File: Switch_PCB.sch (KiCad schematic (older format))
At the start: 53 parts, among them J1 Black, J10 Black, J11 Red, J12-1 Jack 2.1mm, J12-2 Jack 2.1mm, J13 Black, J14 Red, J15 Black, J16 Red, J17 Black, J18 Red, J19 Black, J2 Red, J20 Red, J21 Black, J22 Red, J23 Black, J24 Red, J25 Black, J26 Red, J27 Black, J28 Red, J3 Black, J4 Red, J5 Black, J6 Red, J7 Black, J8 Red, J9 Red, SW1 Switch On-Off-On, SW2 Switch On-Off-On, SW3 Switch On-Off-On, SW4 Switch On-Off-On

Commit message: - validation schématique - validation du contour du PCB - validation du placement des composants, verrouillage des empreintes correctement positionnées
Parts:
- added J12-0: Conn_01x02, Connector_PinHeader_2.54mm:PinHeader_1x02_P2.54mm_Horizontal, symbol Connector_Generic:Conn_01x02
- J1, J3, J5, J7: Description GND -> Alim 1 -
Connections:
- net labels added: +5VD, +VDC, GNDD, GNDPWR
- net labels removed: +5V, GND1, GND2
- wire segments 125 -> 128
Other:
- note added: "KiCad Power Flag for DRC"
- note added: "LED\nON"
- note added: "Mounting Holes"
- note added: "OSHW"
- note added: "Open Source Hardware"
- note removed: "KiCad Power DRC"
- moved on the sheet: H1, H2, H3, H4, J12-1, J12-2

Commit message: Update color for each Banana connector to the pcb component placement 3d rendered.
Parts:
- J1, J10, J21, J23, J25, J27, J3, J5, J7: footprint ArnauldDev_Connector_Banana:SCHUTZINGER_SWEB8094AU-SW_4mm_Horizontal -> ArnauldDev_Connector_Banana:SCHUTZINGER_SWEB8094AU-SW_4mm_Horizontal_Black
- J11, J2, J22, J24, J26, J28, J4, J6, J8, J9: footprint ArnauldDev_Connector_Banana:SCHUTZINGER_SWEB8094AU-SW_4mm_Horizontal -> ArnauldDev_Connector_Banana:SCHUTZINGER_SWEB8094AU-SW_4mm_Horizontal_Red
- J13, J15, J17, J19: footprint ArnauldDev_Connector_Banana:STAUBLI_66.9032-21_XELA-4_4mm_Vertical -> ArnauldDev_Connector_Banana:STAUBLI_66.9032-21_XELA-4_4mm_Vertical_Black
- J14, J16, J18, J20: footprint ArnauldDev_Connector_Banana:STAUBLI_66.9032-21_XELA-4_4mm_Vertical -> ArnauldDev_Connector_Banana:STAUBLI_66.9032-21_XELA-4_4mm_Vertical_Red

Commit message: - Add 3 pin conn for LED states - Start of the routing of the tracks of the electronic card
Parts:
- added J13, J14, J15, J16: Conn_01x03, Connector_PinHeader_2.54mm:PinHeader_1x03_P2.54mm_Vertical, symbol Connector_Generic:Conn_01x03
- J1, J10, J3, J5, J7: symbol Connector_Generic:Conn_01x01 -> Connector:Conn_Coaxial
- J11, J2, J4, J6, J8, J9: footprint ArnauldDev_Connector_Banana:SCHUTZINGER_SWEB8094AU-SW_4mm_Horizontal_Red -> ArnauldDev_Connector_Banana:SCHUTZINGER_SWEB8094AU-RT_4mm_Horizontal_Red; symbol Connector_Generic:Conn_01x01 -> Connector:Conn_Coaxial
- J19: renamed from J13; symbol Connector_Generic:Conn_01x01 -> Connector:Conn_Coaxial
- J20: renamed from J14; footprint ArnauldDev_Connector_Banana:STAUBLI_66.9032-21_XELA-4_4mm_Vertical_Red -> ArnauldDev_Connector_Banana:STAUBLI_66.9032-22_XELA-4_4mm_Vertical_Red; symbol Connector_Generic:Conn_01x01 -> Connector:Conn_Coaxial
- J21: renamed from J15; symbol Connector_Generic:Conn_01x01 -> Connector:Conn_Coaxial
- J22: renamed from J16; footprint ArnauldDev_Connector_Banana:STAUBLI_66.9032-21_XELA-4_4mm_Vertical_Red -> ArnauldDev_Connector_Banana:STAUBLI_66.9032-22_XELA-4_4mm_Vertical_Red; symbol Connector_Generic:Conn_01x01 -> Connector:Conn_Coaxial
- J23: renamed from J17; symbol Connector_Generic:Conn_01x01 -> Connector:Conn_Coaxial
- J24: renamed from J18; footprint ArnauldDev_Connector_Banana:STAUBLI_66.9032-21_XELA-4_4mm_Vertical_Red -> ArnauldDev_Connector_Banana:STAUBLI_66.9032-22_XELA-4_4mm_Vertical_Red; symbol Connector_Generic:Conn_01x01 -> Connector:Conn_Coaxial
- J25: renamed from J19; symbol Connector_Generic:Conn_01x01 -> Connector:Conn_Coaxial
- J26: renamed from J20; footprint ArnauldDev_Connector_Banana:STAUBLI_66.9032-21_XELA-4_4mm_Vertical_Red -> ArnauldDev_Connector_Banana:STAUBLI_66.9032-22_XELA-4_4mm_Vertical_Red; symbol Connector_Generic:Conn_01x01 -> Connector:Conn_Coaxial
- J27: renamed from J21; symbol Connector_Generic:Conn_01x01 -> Connector:Conn_Coaxial
- J28: renamed from J22; footprint ArnauldDev_Connector_Banana:SCHUTZINGER_SWEB8094AU-SW_4mm_Horizontal_Red -> ArnauldDev_Connector_Banana:SCHUTZINGER_SWEB8094AU-RT_4mm_Horizontal_Red; symbol Connector_Generic:Conn_01x01 -> Connector:Conn_Coaxial
- J29: renamed from J23; symbol Connector_Generic:Conn_01x01 -> Connector:Conn_Coaxial
- J30: renamed from J24; footprint ArnauldDev_Connector_Banana:SCHUTZINGER_SWEB8094AU-SW_4mm_Horizontal_Red -> ArnauldDev_Connector_Banana:SCHUTZINGER_SWEB8094AU-RT_4mm_Horizontal_Red; symbol Connector_Generic:Conn_01x01 -> Connector:Conn_Coaxial
- J31: renamed from J25; symbol Connector_Generic:Conn_01x01 -> Connector:Conn_Coaxial
- J32: renamed from J26; footprint ArnauldDev_Connector_Banana:SCHUTZINGER_SWEB8094AU-SW_4mm_Horizontal_Red -> ArnauldDev_Connector_Banana:SCHUTZINGER_SWEB8094AU-RT_4mm_Horizontal_Red; symbol Connector_Generic:Conn_01x01 -> Connector:Conn_Coaxial
- J33: renamed from J27; symbol Connector_Generic:Conn_01x01 -> Connector:Conn_Coaxial
- J34: renamed from J28; footprint ArnauldDev_Connector_Banana:SCHUTZINGER_SWEB8094AU-SW_4mm_Horizontal_Red -> ArnauldDev_Connector_Banana:SCHUTZINGER_SWEB8094AU-RT_4mm_Horizontal_Red; symbol Connector_Generic:Conn_01x01 -> Connector:Conn_Coaxial
- renumbered J12-0 to J12, J12-1 to J17, J12-2 to J18
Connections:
- net GNDD: now also J13.1 (Pin_1), J14.1 (Pin_1), J15.1 (Pin_1), J16.1 (Pin_1)
- net GNDPWR: now also J1.2 (Ext), J10.2 (Ext), J11.2 (Ext), J19.2 (Ext), J2.2 (Ext), J20.2 (Ext), J21.2 (Ext), J22.2 (Ext), J23.2 (Ext), J24.2 (Ext), J25.2 (Ext), J26.2 (Ext), J27.2 (Ext), J28.2 (Ext), J29.2 (Ext), J3.2 (Ext), J30.2 (Ext), J31.2 (Ext), J32.2 (Ext), J33.2 (Ext), J34.2 (Ext), J4.2 (Ext), J5.2 (Ext), J6.2 (Ext), J7.2 (Ext), J8.2 (Ext), J9.2 (Ext)
- net at R1.2, SW1.1 (A): now also J13.2 (Pin_2)
- net at R2.2, SW1.3 (C): now also J13.3 (Pin_3)
- net at R3.2, SW2.1 (A): now also J14.2 (Pin_2)
- net at R4.2, SW2.3 (C): now also J14.3 (Pin_3)
- net at R5.2, SW3.1 (A): now also J15.2 (Pin_2)
- net at R6.2, SW3.3 (C): now also J15.3 (Pin_3)
- net at R7.2, SW4.1 (A): now also J16.2 (Pin_2)
- net at R8.2, SW4.3 (C): now also J16.3 (Pin_3)
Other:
- moved on the sheet: D1, D2, D3, D4, D5, D6, D7, D8, R1, R2, R3, R4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

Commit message: Create local components library
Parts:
- SW1, SW2, SW3, SW4: footprint ArnauldDev_Button_Switch_THT:SW_TME_1MD3T1B1M1QE_DPDT_Straight -> Local_Button_Switch_THT:SW_TME_1MD3T1B1M1QE_DPDT_Straight
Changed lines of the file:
@@
 F 0 "SW3" V 5846 2462 50  0001 R CNN
 F 1 "Switch On-Off-On" V 5100 3350 50  0000 R CNN
-F 2 "ArnauldDev_Button_Switch_THT:SW_TME_1MD3T1B1M1QE_DPDT_Straight" H 5800 3050 50  0001 C CNN
+F 2 "Local_Button_Switch_THT:SW_TME_1MD3T1B1M1QE_DPDT_Straight" H 5800 3050 50  0001 C CNN
 F 3 "https://datasheet.octopart.com/401692-RS-Pro-datasheet-110811736.pdf" H 5800 3050 50  0001 C CNN
 F 4 "Switch of Alim 3" H 5800 2850 50  0001 C CNN "Description"
@@
 F 0 "SW4" V 7346 3198 50  0001 L CNN
 F 1 "Switch On-Off-On" V 6600 3350 50  0000 R CNN
-F 2 "ArnauldDev_Button_Switch_THT:SW_TME_1MD3T1B1M1QE_DPDT_Straight" H 7300 3050 50  0001 C CNN
+F 2 "Local_Button_Switch_THT:SW_TME_1MD3T1B1M1QE_DPDT_Straight" H 7300 3050 50  0001 C CNN
 F 3 "https://datasheet.octopart.com/401692-RS-Pro-datasheet-110811736.pdf" H 7300 3050 50  0001 C CNN
 F 4 "Switch of Alim 4" H 7300 2850 50  0001 C CNN "Description"
@@
 F 0 "SW2" V 4346 3198 50  0001 L CNN
 F 1 "Switch On-Off-On" V 3600 2650 50  0000 L CNN
-F 2 "ArnauldDev_Button_Switch_THT:SW_TME_1MD3T1B1M1QE_DPDT_Straight" H 4300 3050 50  0001 C CNN
+F 2 "Local_Button_Switch_THT:SW_TME_1MD3T1B1M1QE_DPDT_Straight" H 4300 3050 50  0001 C CNN
 F 3 "https://datasheet.octopart.com/401692-RS-Pro-datasheet-110811736.pdf" H 4300 3050 50  0001 C CNN
 F 4 "Switch of Alim 2" H 4300 2850 50  0001 C CNN "Description"
@@
 F 0 "SW1" V 2846 2462 50  0001 R CNN
 F 1 "Switch On-Off-On" V 2100 3350 50  0000 R CNN
-F 2 "ArnauldDev_Button_Switch_THT:SW_TME_1MD3T1B1M1QE_DPDT_Straight" H 2800 3050 50  0001 C CNN
+F 2 "Local_Button_Switch_THT:SW_TME_1MD3T1B1M1QE_DPDT_Straight" H 2800 3050 50  0001 C CNN
 F 3 "https://datasheet.octopart.com/401692-RS-Pro-datasheet-110811736.pdf" H 2800 3050 50  0001 C CNN
 F 4 "1MD3T1B1M1QE" H 2800 2850 50  0001 C CNN "Manufacturer Part Number"

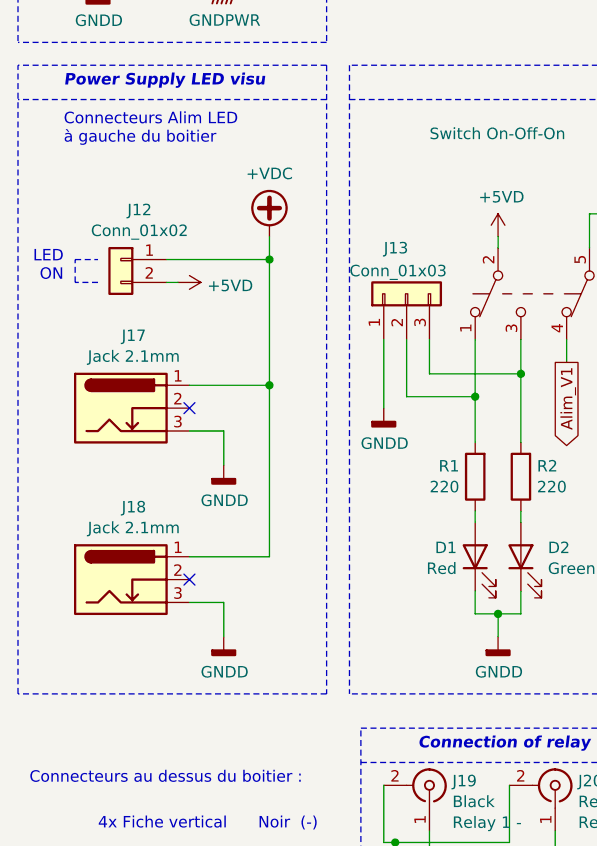
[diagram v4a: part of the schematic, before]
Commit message: Update local inter footprint SW_TME_1MD3T1B1M1QE_DPDT_Straight.kicad_mod, change for oblong hole. Add packages3D in kicad_local_mod folder.
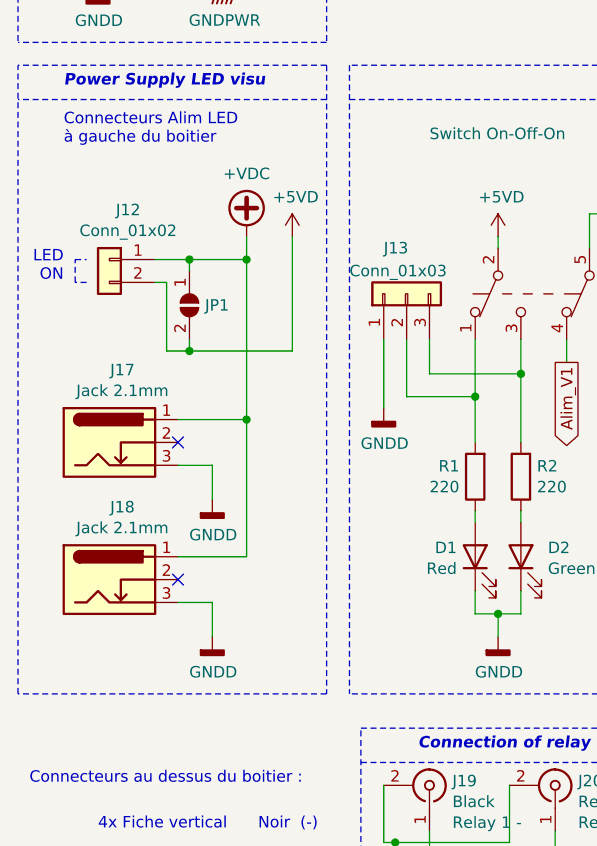
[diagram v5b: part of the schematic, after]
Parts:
- added JP1: SolderJumper_2_Open, Jumper:SolderJumper-2_P1.3mm_Open_TrianglePad1.0x1.5mm, symbol Jumper:SolderJumper_2_Open
- J1, J10, J27, J29, J3, J31, J33, J5, J7: footprint ArnauldDev_Connector_Banana:SCHUTZINGER_SWEB8094AU-SW_4mm_Horizontal_Black -> Local_Connector_Banana:SCHUTZINGER_SWEB8094AU-SW_4mm_Horizontal_Black
- J11, J2, J28, J30, J32, J34, J4, J6, J8, J9: footprint ArnauldDev_Connector_Banana:SCHUTZINGER_SWEB8094AU-RT_4mm_Horizontal_Red -> Local_Connector_Banana:SCHUTZINGER_SWEB8094AU-RT_4mm_Horizontal_Red
- J17, J18: footprint ArnauldDev_Connector_BarrelJack:BarrelJack_FC681465P_Pin3_Horizontal -> Local_Connector_BarrelJack:BarrelJack_FC681465P_Pin3_Horizontal
- J19, J21, J23, J25: footprint ArnauldDev_Connector_Banana:STAUBLI_66.9032-21_XELA-4_4mm_Vertical_Black -> Local_Connector_Banana:STAUBLI_66.9032-21_XELA-4_4mm_Vertical_Black
- J20, J22, J24, J26: footprint ArnauldDev_Connector_Banana:STAUBLI_66.9032-22_XELA-4_4mm_Vertical_Red -> Local_Connector_Banana:STAUBLI_66.9032-22_XELA-4_4mm_Vertical_Red
- R1, R2, R3, R4, R5, R6, R7, R8: footprint Resistor_SMD:R_1206_3216Metric_Pad1.42x1.75mm_HandSolder -> Resistor_SMD:R_1206_3216Metric_Pad1.30x1.75mm_HandSolder
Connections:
- net +5VD: now also JP1.2 (B)
- net +VDC: now also JP1.1 (A)
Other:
- moved on the sheet: J12, J17, J18

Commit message: Update project Add layers number
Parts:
- D1, D2, D3, D4, D5, D6, D7, D8: symbol Device:LED -> Switch_PCB-rescue:LED-Device
- H1, H2, H3, H4: symbol Mechanical:MountingHole_Pad -> Switch_PCB-rescue:MountingHole_Pad-Mechanical
- J1, J10, J11, J19, J2, J20, J21, J22, J23, J24, J25, J26, J27, J28, J29, J3, J30, J31, J32, J33, J34, J4, J5, J6, J7, J8, J9: symbol Connector:Conn_Coaxial -> Switch_PCB-rescue:Conn_Coaxial-Connector
- J12: symbol Connector_Generic:Conn_01x02 -> Switch_PCB-rescue:Conn_01x02-Connector_Generic
- J13, J14, J15, J16: symbol Connector_Generic:Conn_01x03 -> Switch_PCB-rescue:Conn_01x03-Connector_Generic
- J17, J18: symbol Connector:Barrel_Jack_Switch_Pin3Ring -> Switch_PCB-rescue:Barrel_Jack_Switch_Pin3Ring-Connector
- JP1: symbol Jumper:SolderJumper_2_Open -> Switch_PCB-rescue:SolderJumper_2_Open-Jumper
- R1, R2, R3, R4, R5, R6, R7, R8: symbol Device:R -> Switch_PCB-rescue:R-Device
- SW1, SW2, SW3, SW4: symbol Switch:SW_Push_DPDT -> Switch_PCB-rescue:SW_Push_DPDT-Switch

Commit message: Change LED 3mm with 15.2mm Leads for 18 mm high * LED_D3.0mm_H18.0mm_Red * LED_D3.0mm_H18.0mm_Green
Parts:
- D1, D3, D5, D7: footprint LED_THT:LED_D3.0mm -> Local_LED_THT:LED_D3.0mm_H18.0mm_Red
- D2, D4, D6, D8: footprint LED_THT:LED_D3.0mm -> Local_LED_THT:LED_D3.0mm_H18.0mm_Green
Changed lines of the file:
@@
 Sheet 1 1
 Title "Power switch for test bench"
-Date "2020-09-24"
-Rev "0.1.0"
+Date "2020-10-11"
+Rev "0.1.1"
 Comp "Laboratoire LAPLACE"
 Comment1 "www.laplace.univ-tlse.fr"
@@
 F 0 "D1" V 2539 4080 50  0000 L CNN
 F 1 "Red" V 2448 4080 50  0000 L CNN
-F 2 "LED_THT:LED_D3.0mm" H 2500 4000 50  0001 C CNN
+F 2 "Local_LED_THT:LED_D3.0mm_H18.0mm_Red" H 2500 4000 50  0001 C CNN
 F 3 "https://docs.rs-online.com/5919/0900766b813955e6.pdf" H 2500 4000 50  0001 C CNN
 F 4 "LED Alim 1" H 2500 4000 50  0001 C CNN "Description"
@@
 F 0 "D7" V 7039 4079 50  0000 L CNN
 F 1 "Red" V 6948 4079 50  0000 L CNN
-F 2 "LED_THT:LED_D3.0mm" H 7000 4000 50  0001 C CNN
+F 2 "Local_LED_THT:LED_D3.0mm_H18.0mm_Red" H 7000 4000 50  0001 C CNN
 F 3 "https://docs.rs-online.com/5919/0900766b813955e6.pdf" H 7000 4000 50  0001 C CNN
 F 4 "LED Alim 4" H 7000 4000 50  0001 C CNN "Description"
@@
 F 0 "D8" V 7239 3882 50  0000 R CNN
 F 1 "Green" V 7148 3882 50  0000 R CNN
-F 2 "LED_THT:LED_D3.0mm" H 7200 4000 50  0001 C CNN
+F 2 "Local_LED_THT:LED_D3.0mm_H18.0mm_Green" H 7200 4000 50  0001 C CNN
 F 3 "https://docs.rs-online.com/c1ec/0900766b813955e9.pdf" H 7200 4000 50  0001 C CNN
 F 4 "LED Keith VB2" H 7200 4000 50  0001 C CNN "Description"
@@
 F 0 "D6" V 5739 3882 50  0000 R CNN
 F 1 "Green" V 5648 3882 50  0000 R CNN
-F 2 "LED_THT:LED_D3.0mm" H 5700 4000 50  0001 C CNN
+F 2 "Local_LED_THT:LED_D3.0mm_H18.0mm_Green" H 5700 4000 50  0001 C CNN
 F 3 "https://docs.rs-online.com/c1ec/0900766b813955e9.pdf" H 5700 4000 50  0001 C CNN
 F 4 "LED Keith VB1" H 5700 4000 50  0001 C CNN "Description"
@@
 F 0 "D5" V 5539 4079 50  0000 L CNN
 F 1 "Red" V 5448 4079 50  0000 L CNN
-F 2 "LED_THT:LED_D3.0mm" H 5500 4000 50  0001 C CNN
+F 2 "Local_LED_THT:LED_D3.0mm_H18.0mm_Red" H 5500 4000 50  0001 C CNN
 F 3 "https://docs.rs-online.com/5919/0900766b813955e6.pdf" H 5500 4000 50  0001 C CNN
 F 4 "LED Alim 3" H 5500 4000 50  0001 C CNN "Description"
@@
 F 0 "D4" V 4239 3882 50  0000 R CNN
 F 1 "Green" V 4148 3882 50  0000 R CNN
-F 2 "LED_THT:LED_D3.0mm" H 4200 4000 50  0001 C CNN
+F 2 "Local_LED_THT:LED_D3.0mm_H18.0mm_Green" H 4200 4000 50  0001 C CNN
 F 3 "https://docs.rs-online.com/c1ec/0900766b813955e9.pdf" H 4200 4000 50  0001 C CNN
 F 4 "LED Keith VA2" H 4200 4000 50  0001 C CNN "Description"
@@
 F 0 "D3" V 4039 4080 50  0000 L CNN
 F 1 "Red" V 3948 4080 50  0000 L CNN
-F 2 "LED_THT:LED_D3.0mm" H 4000 4000 50  0001 C CNN
+F 2 "Local_LED_THT:LED_D3.0mm_H18.0mm_Red" H 4000 4000 50  0001 C CNN
 F 3 "https://docs.rs-online.com/5919/0900766b813955e6.pdf" H 4000 4000 50  0001 C CNN
 F 4 "LED Alim 2" H 4000 4000 50  0001 C CNN "Description"
@@
 F 0 "D2" V 2739 3882 50  0000 R CNN
 F 1 "Green" V 2648 3882 50  0000 R CNN
-F 2 "LED_THT:LED_D3.0mm" H 2700 4000 50  0001 C CNN
+F 2 "Local_LED_THT:LED_D3.0mm_H18.0mm_Green" H 2700 4000 50  0001 C CNN
 F 3 "https://docs.rs-online.com/c1ec/0900766b813955e9.pdf" H 2700 4000 50  0001 C CNN
 F 4 "LED Keith VA1" H 2700 4000 50  0001 C CNN "Description"
